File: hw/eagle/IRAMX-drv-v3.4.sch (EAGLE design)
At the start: 175 parts, among them IC1 IRAMX16UP60B, IC10 TCA0372DWDM2, IC12 SI8621, IC13 AM26LS32ACD, IC14 rk-2415s, IC2 STM32F103R6T, IC3 LD117AS33TR, IC4 LD117AS33TR, IC5 STM32F405RGT, IC6 78, IC7 7812TV, IC8 ADM485SOIC8, IC9 ADM485SOIC8, J1 22-27-2031-03, Q1 IRLML6344, Q2 8M, Q3 IRLML6344, Q4 8M

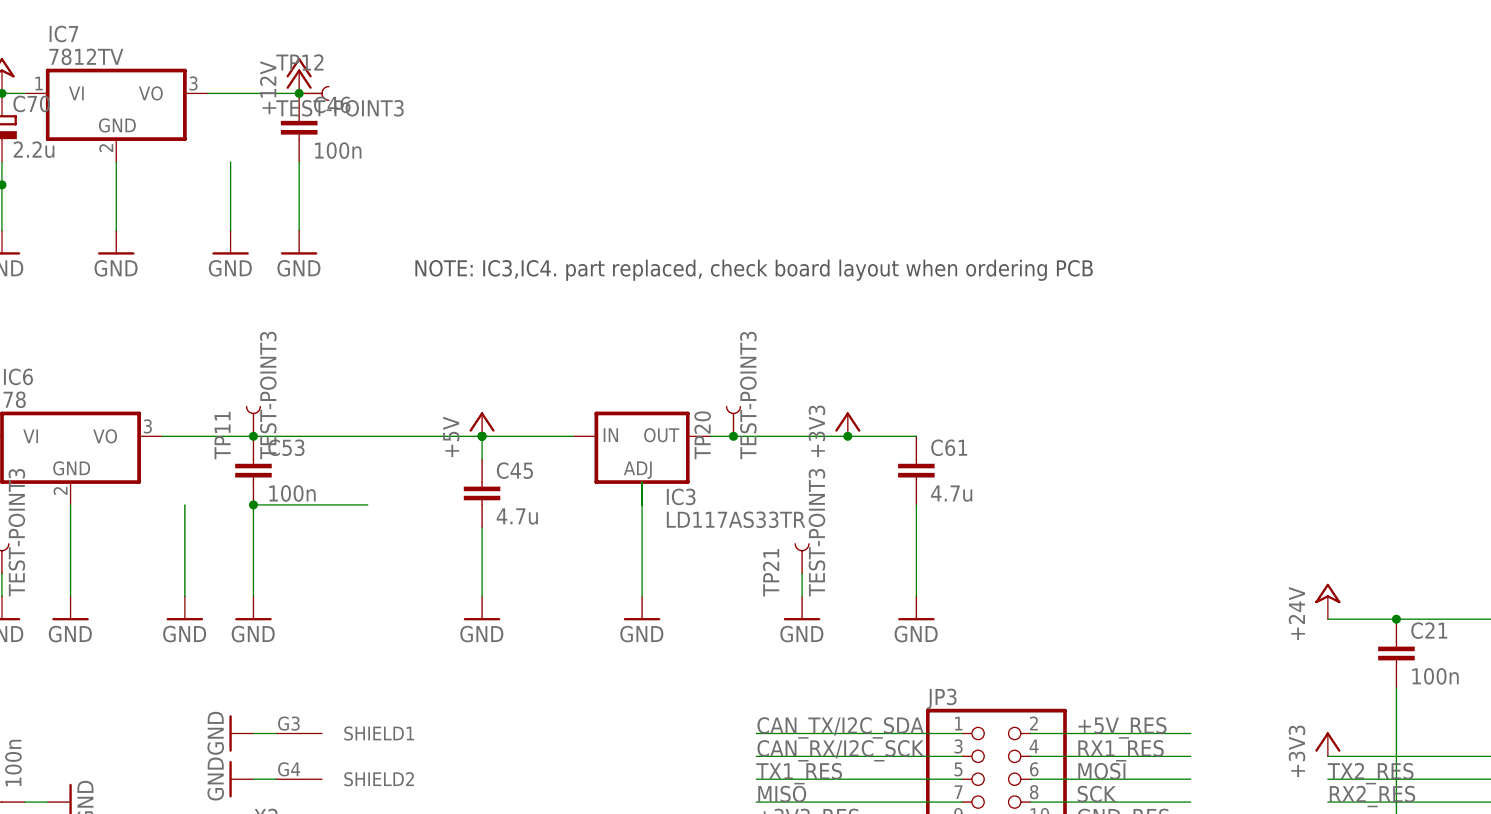
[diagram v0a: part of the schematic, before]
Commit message: fixed 3v3 regulator footprint
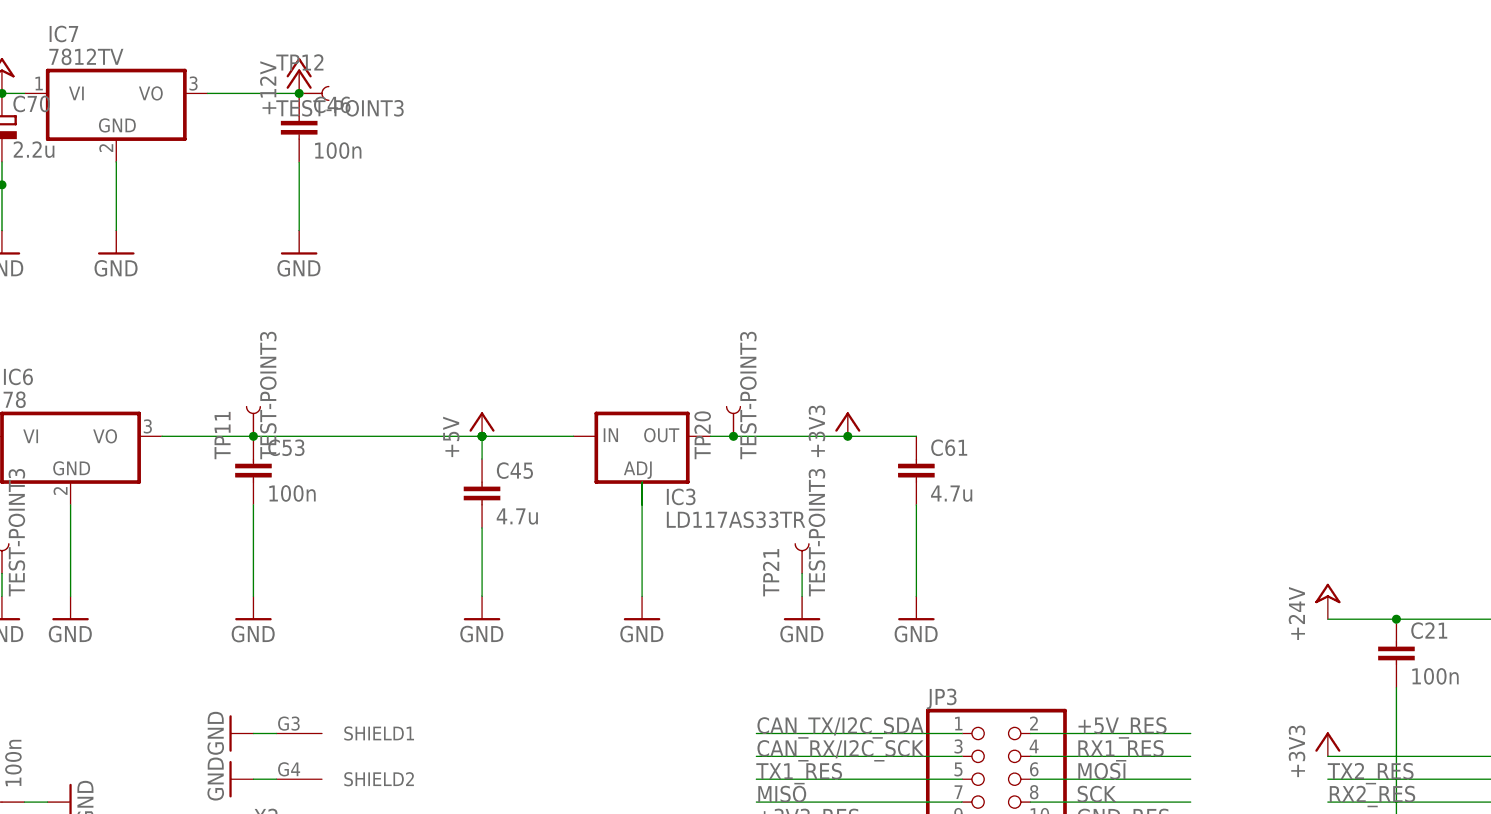
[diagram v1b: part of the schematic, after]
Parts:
- IC3, IC4: device v-reg:LD117AS33TR -> reroolib:LD117AS33TR
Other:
- note removed: "NOTE: IC3,IC4. part replaced, check board layout when ordering PCB"
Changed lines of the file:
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@@
 <?xml version="1.0" encoding="utf-8"?>
 <!DOCTYPE eagle SYSTEM "eagle.dtd">
-<eagle version="7.5.0">
+<eagle version="7.2.0">
 <drawing>
 <settings>
@@
 <part name="C46" library="rcl" deviceset="C-EU" device="C0603" value="100n"/>
 <part name="GND25" library="supply1" deviceset="GND" device=""/>
-<part name="GND28" library="supply1" deviceset="GND" device=""/>
 <part name="GND29" library="supply1" deviceset="GND" device=""/>
 <part name="GND30" library="supply1" deviceset="GND" device=""/>
 <part name="GND31" library="supply1" deviceset="GND" device=""/>
-<part name="GND33" library="supply1" deviceset="GND" device=""/>
 <part name="GND34" library="supply1" deviceset="GND" device=""/>
 <part name="GND35" library="supply1" deviceset="GND" device=""/>
@@
 <part name="LOGO1" library="SparkFun-Aesthetics" deviceset="OSHW-LOGO" device="L"/>
 <part name="GND68" library="supply1" deviceset="GND" device=""/>
-<part name="IC3" library="v-reg" deviceset="LD117A?*" device="S" technology="33TR"/>
-<part name="IC4" library="v-reg" deviceset="LD117A?*" device="S" technology="33TR"/>
+<part name="IC3" library="reroolib" deviceset="LD117A?*" device="S" technology="33TR"/>
+<part name="IC4" library="reroolib" deviceset="LD117A?*" device="S" technology="33TR"/>
 </parts>
 <sheets>
 <sheet>
 <plain>
-<text x="-182.88" y="147.32" size="1.778" layer="97">NOTE: IC3,IC4. part replaced, check board layout when ordering PCB</text>
 </plain>
 <instances>
@@
 <instance part="C46" gate="G$1" x="-195.58" y="165.1"/>
 <instance part="GND25" gate="1" x="-215.9" y="149.86"/>
-<instance part="GND28" gate="1" x="-203.2" y="149.86"/>
 <instance part="GND29" gate="1" x="-195.58" y="149.86"/>
 <instance part="GND30" gate="1" x="-228.6" y="149.86"/>
 <instance part="GND31" gate="1" x="-200.66" y="109.22"/>
-<instance part="GND33" gate="1" x="-208.28" y="109.22"/>
 <instance part="GND34" gate="1" x="-220.98" y="109.22"/>
 <instance part="GND35" gate="1" x="-236.22" y="109.22"/>
@@
 </segment>
 <segment>
-<pinref part="GND28" gate="1" pin="GND"/>
-<wire x1="-203.2" y1="160.02" x2="-203.2" y2="152.4" width="0.1524" layer="91"/>
-</segment>
-<segment>
 <pinref part="C46" gate="G$1" pin="2"/>
 <pinref part="GND29" gate="1" pin="GND"/>
@@
 </segment>
 <segment>
-<pinref part="GND33" gate="1" pin="GND"/>
-<wire x1="-208.28" y1="121.92" x2="-208.28" y2="111.76" width="0.1524" layer="91"/>
-</segment>
-<segment>
 <pinref part="C53" gate="G$1" pin="2"/>
 <pinref part="GND31" gate="1" pin="GND"/>
 <wire x1="-200.66" y1="121.92" x2="-200.66" y2="111.76" width="0.1524" layer="91"/>
-<wire x1="-187.96" y1="121.92" x2="-200.66" y2="121.92" width="0.1524" layer="91"/>
-<junction x="-200.66" y="121.92"/>
-</segment>
-<segment>
+</segment>
+<segment>

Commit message: name signals
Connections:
- net N$13 renamed VCAP2
- net N$14 renamed VCAP1
- net N$15 renamed OSC_OUT
- net N$22 renamed USB_DP_
- net N$23 renamed USB_DM_
- net N$39 renamed OSC_IN
- net N$4 renamed PA5
- net N$46 renamed VDDA
- net N$49 renamed PA6
- net N$51 renamed PA7
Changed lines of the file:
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@@
 <?xml version="1.0" encoding="utf-8"?>
 <!DOCTYPE eagle SYSTEM "eagle.dtd">
-<eagle version="7.2.0">
+<eagle version="7.7.0">
 <drawing>
 <settings>
@@
 </segment>
 </net>
-<net name="N$15" class="0">
+<net name="OSC_OUT" class="0">
 <segment>
 <pinref part="C44" gate="G$1" pin="2"/>
@@
 </segment>
 </net>
-<net name="N$39" class="0">
+<net name="OSC_IN" class="0">
 <segment>
 <pinref part="C43" gate="G$1" pin="2"/>
@@
 <pinref part="C56" gate="G$1" pin="2"/>
 <pinref part="P+7" gate="1" pin="+5V"/>
-<pinref part="P+7" gate="1" pin="+5V"/>
 <wire x1="-248.92" y1="-22.86" x2="-254" y2="-22.86" width="0.1524" layer="91"/>
 <junction x="-254" y="-22.86"/>
@@
 <pinref part="R17" gate="G$1" pin="2"/>
 <pinref part="C55" gate="G$1" pin="2"/>
-<pinref part="P+6" gate="1" pin="+5V"/>
 <pinref part="P+6" gate="1" pin="+5V"/>
 <wire x1="-248.92" y1="17.78" x2="-254" y2="17.78" width="0.1524" layer="91"/>
@@
 </segment>
 </net>
-<net name="N$13" class="0">
+<net name="VCAP2" class="0">
 <segment>
 <pinref part="C58" gate="G$1" pin="2"/>
@@
 </segment>
 </net>
-<net name="N$14" class="0">
+<net name="VCAP1" class="0">
 <segment>
 <pinref part="IC5" gate="MCU" pin="VCAP1"/>
@@
 </segment>
 </net>
-<net name="N$46" class="0">
+<net name="VDDA" class="0">
 <segment>
 <pinref part="C31" gate="G$1" pin="2"/>
@@
 </segment>
 </net>
-<net name="N$22" class="0">
+<net name="USB_DP_" class="0">
 <segment>
 <pinref part="IC5" gate="MCU" pin="PA12"/>
@@
 </segment>
 </net>
-<net name="N$23" class="0">
+<net name="USB_DM_" class="0">
 <segment>
 <pinref part="IC5" gate="MCU" pin="PA11"/>
@@
 </segment>
 </net>
-<net name="N$4" class="0">
+<net name="PA5" class="0">
 <segment>
 <pinref part="IC2" gate="MCU" pin="PA5"/>
@@
 </segment>
 </net>
-<net name="N$49" class="0">
+<net name="PA6" class="0">
 <segment>
 <pinref part="IC2" gate="MCU" pin="PA6"/>
@@
 </segment>
 </net>
-<net name="N$51" class="0">
+<net name="PA7" class="0">
 <segment>
 <pinref part="IC2" gate="MCU" pin="PA7"/>
